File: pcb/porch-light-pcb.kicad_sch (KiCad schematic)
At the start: 1 part

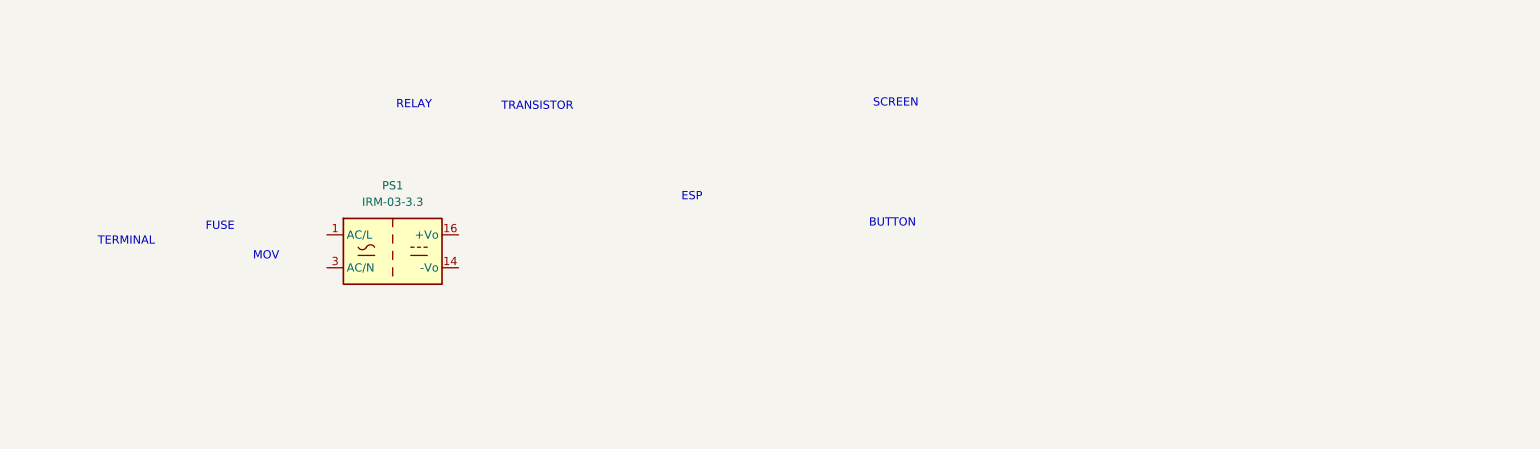
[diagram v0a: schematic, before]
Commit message: esp32 symbol and footprint
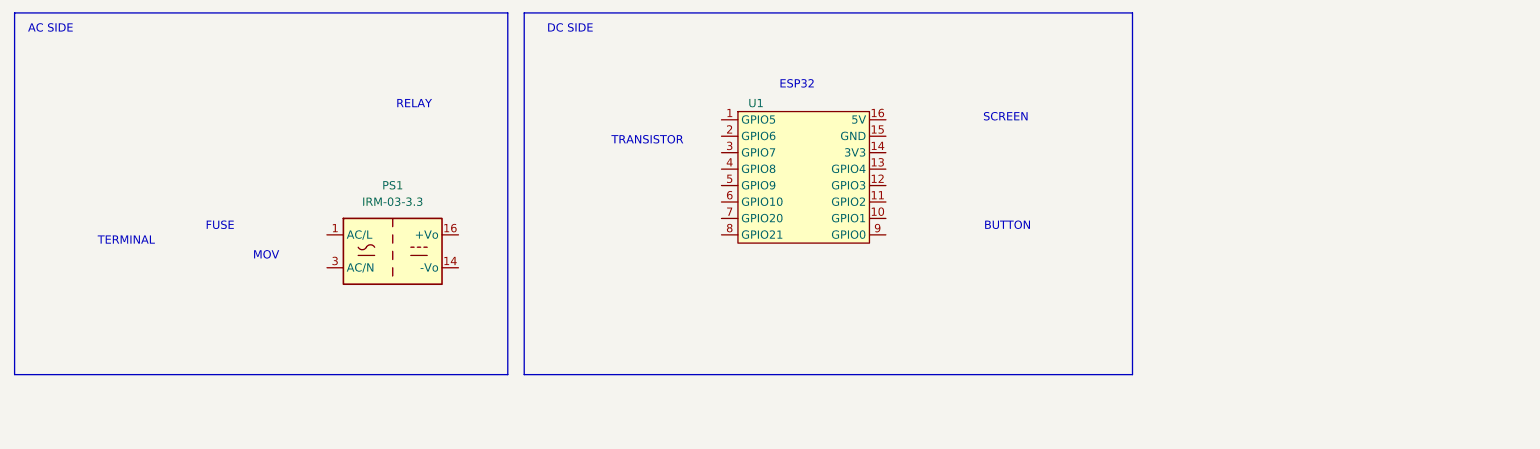
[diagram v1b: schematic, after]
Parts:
- added U1: ~, TENSTAR:TENSTAR_ESP32-C3-SUPERMINI, symbol TENSTAR:TENSTAR_ESP32-C3-SUPERMINI
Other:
- note added: "AC SIDE"
- note added: "DC SIDE"
- note added: "ESP32"
- note removed: "ESP"
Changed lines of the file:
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@@
 	(generator_version "9.0")
 	(paper "A4")
+	(rectangle
+		(start 92.71 12.7)
+		(end 186.69 68.58)
+		(stroke
+			(width 0)
+			(type default)
+		)
+		(fill
+			(type none)
+		)
+	)
+	(rectangle
+		(start 13.97 12.7)
+		(end 90.17 68.58)
+		(stroke
+			(width 0)
+			(type default)
+		)
+		(fill
+			(type none)
+		)
+	)
 	(text "FUSE"
 		(exclude_from_sim no)
@@
 		)
 	)
+	(text "DC SIDE\n"
+		(exclude_from_sim no)
+		(at 99.822 15.24 0)
+		(effects
+			(font
+				(size 1.27 1.27)
+			)
+		)
+	)
 	(text "MOV"
 		(exclude_from_sim no)
@@
 	(text "TRANSISTOR"
 		(exclude_from_sim no)
-		(at 94.742 27.178 0)
+		(at 111.76 32.512 0)
+		(effects
+			(font
+				(size 1.27 1.27)
+			)
+		)
+	)
+	(text "AC SIDE\n"
+		(exclude_from_sim no)
+		(at 19.558 15.24 0)
 		(effects
 			(font
@@
 	(text "SCREEN"
 		(exclude_from_sim no)
-		(at 150.114 26.67 0)
-		(effects
-			(font
-				(size 1.27 1.27)
-			)
-		)
-	)
-	(text "ESP\n"
-		(exclude_from_sim no)
-		(at 118.618 41.148 0)
+		(at 167.132 28.956 0)
+		(effects
+			(font
+				(size 1.27 1.27)
+			)
+		)
+	)
+	(text "ESP32"
+		(exclude_from_sim no)
+		(at 134.874 23.876 0)
 		(effects
 			(font
@@
 	(text "BUTTON\n"
 		(exclude_from_sim no)
-		(at 149.606 45.212 0)
-		(effects
-			(font
-				(size 1.27 1.27)
-			)
-		)
+		(at 167.386 45.72 0)
+		(effects
+			(font
+				(size 1.27 1.27)
+			)
+		)
+	)
+	(symbol
+		(lib_id "TENSTAR:TENSTAR_ESP32-C3-SUPERMINI")
+		(at 135.89 39.37 0)
+		(unit 1)
+		(exclude_from_sim no)
+		(in_bom yes)
+		(on_board yes)
+		(dnp no)
+		(property "Reference" "U1"
+			(at 128.524 26.67 0)
+			(effects
+				(font
+					(size 1.27 1.27)
+				)
+			)
+		)
+		(property "Value" "~"
+			(at 135.89 26.416 0)
+			(effects
+				(font
+					(size 1.27 1.27)
+				)
+				(hide yes)
+			)
+		)
+		(property "Footprint" "TENSTAR:TENSTAR_ESP32-C3-SUPERMINI"
+			(at 135.89 53.086 0)
+			(effects
+				(font
+					(size 1.27 1.27)
+				)
+				(hide yes)
+			)
+		)
+		(property "Datasheet" "https://www.waveshare.com/wiki/ESP32-C3-Zero"
+			(at 135.636 55.626 0)
+			(effects
+				(font
+					(size 1.27 1.27)
+				)
+				(hide yes)
+			)
+		)
+		(property "Description" ""
+			(at 125.73 29.21 0)
+			(effects
+				(font
+					(size 1.27 1.27)
+				)
+				(hide yes)
+			)
+		)
+		(pin "8"
+		)
+		(pin "6"
+		)
+		(pin "14"
+		)
+		(pin "7"
+		)
+		(pin "2"
+		)
+		(pin "1"
+		)
+		(pin "13"
+		)
+		(pin "4"
+		)
+		(pin "11"
+		)
+		(pin "3"
+		)
+		(pin "10"
+		)
+		(pin "12"
+		)
+		(pin "5"
+		)
+		(pin "15"
+		)
+		(pin "9"
+		)
+		(pin "16"
+		)
+		(instances
+			(project "porch-light-pcb"
+				(path "/c90725bf-bd5a-4426-8225-f7c4cfb17e78"
+					(reference "U1")
+					(unit 1)
+				)
+			)
+		)

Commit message: preliminary circuit design
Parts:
- added C1: 220uF, Capacitor_THT:CP_Radial_D5.0mm_P2.50mm, symbol Device:C_Polarized
- added C2: 0.1uF, Capacitor_SMD:C_0603_1608Metric_Pad1.08x0.95mm_HandSolder, symbol Device:C
- added F1: 0HAAL1000-02, symbol Device:Fuse
- added J1: Screw_Terminal_01x02, symbol Connector:Screw_Terminal_01x02
- added J2: Conn_01x02, Connector_PinHeader_2.54mm:PinHeader_1x02_P2.54mm_Vertical, symbol Connector_Generic:Conn_01x02
- added J4: Screw_Terminal_01x01, symbol Connector:Screw_Terminal_01x01
- added K1: PRY2-3V-450-1A-EF, PRY2_3V_450_1A_EF:RELAY_PRY2-3V-450-1A-EF, symbol PRY2-3V-450-1A-EF:PRY2-3V-450-1A-EF
- added Q1: PN2222A, Package_TO_SOT_THT:TO-92_Inline, symbol Transistor_BJT:PN2222A
- added R1: 270R, symbol Device:R_US
- added RV1: V150LA10AP, symbol Device:Varistor
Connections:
- net GND: now reaches U1.15 (GND)
- net GND: now also PS1.14 (-Vo), C1.2, C2.2, J2.2 (Pin_2), Q1.1 (E)
- net +3.3V: now reaches U1.16 (5V)
- net +3.3V: now also PS1.16 (+Vo), C1.1, C2.1, K1.COIL1
- net BUTTON_GPIO: now reaches U1.9 (GPIO0)
- net BUTTON_GPIO: now also J2.1 (Pin_1)
- net at PS1.1 (AC/L): now also F1.2, RV1.1
- net at PS1.3 (AC/N): now also J1.2 (Pin_2), RV1.2
- new net: F1.1, J1.1 (Pin_1), K1.NO
- new net: Q1.2 (B), R1.2
- new net: J4.1 (Pin_1), K1.COM
- new net RELAY_GND: K1.COIL2, Q1.3 (C)
- new net RELAY_GPIO: R1.1
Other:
- note added: "250VAC 2A Slow blow"
- note added: "AC IN"
- note added: "Placed very close to ESP32"
- note added: "TO LIGHT"
- note removed: "FUSE"
- note removed: "MOV"
- note removed: "SCREEN"
- note removed: "TERMINAL"
- moved on the sheet: PS1, U1

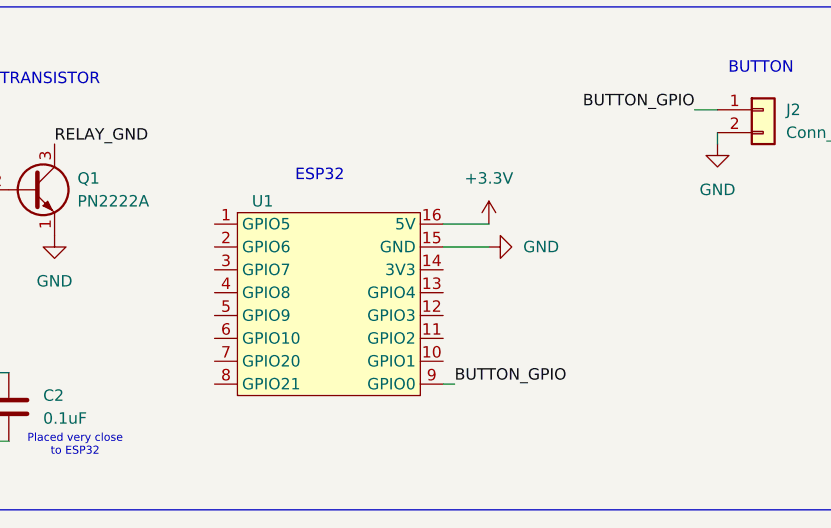
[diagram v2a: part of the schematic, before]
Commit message: relay_gpio connection
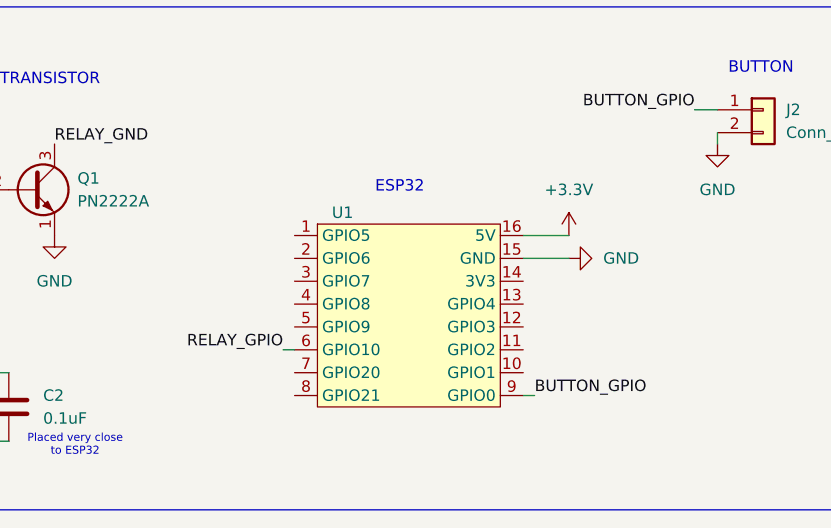
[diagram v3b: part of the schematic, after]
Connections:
- net RELAY_GPIO: now also U1.6 (GPIO10)
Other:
- moved on the sheet: U1
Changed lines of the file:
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@@
 	(text "ESP32"
 		(exclude_from_sim no)
-		(at 160.274 31.496 0)
+		(at 169.164 32.766 0)
 		(effects
 			(font
@@
 	(wire
 		(pts
-			(xy 173.99 36.83) (xy 179.07 36.83)
+			(xy 182.88 38.1) (xy 187.96 38.1)
 		)
 		(stroke
@@
 	(wire
 		(pts
+			(xy 156.21 50.8) (xy 157.48 50.8)
+		)
+		(stroke
+			(width 0)
+			(type default)
+		)
+	)
+	(wire
+		(pts
 			(xy 41.91 53.34) (xy 46.99 53.34)
 		)
@@
 	(wire
 		(pts
-			(xy 173.99 39.37) (xy 179.07 39.37)
+			(xy 182.88 40.64) (xy 187.96 40.64)
 		)
 		(stroke
@@
 	(wire
 		(pts
-			(xy 175.26 54.61) (xy 173.99 54.61)
+			(xy 184.15 55.88) (xy 182.88 55.88)
 		)
 		(stroke
@@
 		)
 	)
+	(label "RELAY_GPIO"
+		(at 156.21 50.8 180)
+		(effects
+			(font
+				(size 1.27 1.27)
+			)
+			(justify right bottom)
+		)
+	)
 	(label "RELAY_GND"
 		(at 130.81 27.94 0)
@@
 	)
 	(label "BUTTON_GPIO"
-		(at 175.26 54.61 0)
+		(at 184.15 55.88 0)
 		(effects
 			(font
@@
 	(symbol
 		(lib_id "power:GND")
-		(at 179.07 39.37 90)
+		(at 187.96 40.64 90)
 		(unit 1)
 		(exclude_from_sim no)
@@
 		(fields_autoplaced yes)
 		(property "Reference" "#PWR06"
-			(at 185.42 39.37 0)
+			(at 194.31 40.64 0)
 			(effects
 				(font
@@
 		)
 		(property "Value" "GND"
-			(at 182.88 39.3699 90)
+			(at 191.77 40.6399 90)
 			(effects
 				(font
@@
 		)
 		(property "Footprint" ""
-			(at 179.07 39.37 0)
+			(at 187.96 40.64 0)
 			(effects
 				(font
@@
 		)
 		(property "Datasheet" ""
-			(at 179.07 39.37 0)
+			(at 187.96 40.64 0)
 			(effects
 				(font
@@
 		)
 		(property "Description" "Power symbol creates a global label with name \"GND\" , ground"
-			(at 179.07 39.37 0)
+			(at 187.96 40.64 0)
 			(effects
 				(font
@@
 	(symbol
 		(lib_id "TENSTAR:TENSTAR_ESP32-C3-SUPERMINI")
-		(at 161.29 46.99 0)
+		(at 170.18 48.26 0)
 		(unit 1)
 		(exclude_from_sim no)
@@
 		(dnp no)
 		(property "Reference" "U1"
-			(at 153.924 34.29 0)
+			(at 162.814 35.56 0)
 			(effects
 				(font
@@
 		)
 		(property "Value" "~"
-			(at 161.29 34.036 0)
+			(at 170.18 35.306 0)
 			(effects
 				(font
@@
 		)
 		(property "Footprint" "TENSTAR:TENSTAR_ESP32-C3-SUPERMINI"
-			(at 161.29 60.706 0)
+			(at 170.18 61.976 0)
 			(effects
 				(font
@@
 		)
 		(property "Datasheet" "https://www.waveshare.com/wiki/ESP32-C3-Zero"
-			(at 161.036 63.246 0)
+			(at 169.926 64.516 0)
 			(effects
 				(font
@@
 		)
 		(property "Description" ""
-			(at 151.13 36.83 0)
+			(at 160.02 38.1 0)
 			(effects
 				(font
@@
 	(symbol
 		(lib_id "power:+3.3V")
-		(at 179.07 36.83 0)
+		(at 187.96 38.1 0)
 		(unit 1)
 		(exclude_from_sim no)
@@
 		(fields_autoplaced yes)
 		(property "Reference" "#PWR05"
-			(at 179.07 40.64 0)
+			(at 187.96 41.91 0)
 			(effects
 				(font
@@
 		)
 		(property "Value" "+3.3V"
-			(at 179.07 31.75 0)
+			(at 187.96 33.02 0)
 			(effects
 				(font
@@
 		)
 		(property "Footprint" ""
-			(at 179.07 36.83 0)
+			(at 187.96 38.1 0)
 			(effects
 				(font
@@
 		)
 		(property "Datasheet" ""
-			(at 179.07 36.83 0)
+			(at 187.96 38.1 0)
 			(effects
 				(font
@@
 		)
 		(property "Description" "Power symbol creates a global label with name \"+3.3V\""
-			(at 179.07 36.83 0)
-			(effects
-				(font
+			(at 187.96 38.1 0)
+			(effects
+				(font

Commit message: terminal block chosen
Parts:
- removed J1: Screw_Terminal_01x02, symbol Connector:Screw_Terminal_01x02
- removed J4: Screw_Terminal_01x01, symbol Connector:Screw_Terminal_01x01
- added J1: HA0300500000G, CONN_HA0300500000G_AMP, symbol 2026-08-06_05-33-22:HA0300500000G
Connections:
- net AC_LIVE: now reaches F1.1, K1.NO
- net AC_LIVE: now also J1.3, J1.4
- net at K1.COM: now also J1.5, J1.6
- net AC_NEUTRAL: now reaches PS1.3 (AC/N), RV1.2
- net AC_NEUTRAL: now also J1.1, J1.2
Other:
- moved on the sheet: C1, C2, F1, J2, K1, PS1, Q1, R1, RV1, U1

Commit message: footprint assignment
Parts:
- F1: footprint (none) -> 0HAAL1000_02:FUSRR508W60L840T400H810B
- J1: footprint CONN_HA0300500000G_AMP -> HA0300500000G:CONN_HA0300500000G_AMP
- R1: footprint (none) -> Resistor_THT:R_Axial_DIN0207_L6.3mm_D2.5mm_P10.16mm_Horizontal
- RV1: footprint (none) -> Varistor:RV_Disc_D15.5mm_W5.4mm_P7.5mm
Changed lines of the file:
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@@
 			)
 		)
-		(property "Footprint" "CONN_HA0300500000G_AMP"
+		(property "Footprint" "HA0300500000G:CONN_HA0300500000G_AMP"
 			(at 30.48 62.23 0)
 			(effects
@@
 			)
 		)
-		(property "Footprint" ""
+		(property "Footprint" "0HAAL1000_02:FUSRR508W60L840T400H810B"
 			(at 57.15 56.388 90)
 			(effects
@@
 			)
 		)
-		(property "Footprint" ""
+		(property "Footprint" "Resistor_THT:R_Axial_DIN0207_L6.3mm_D2.5mm_P10.16mm_Horizontal"
 			(at 138.684 33.274 90)
 			(effects
@@
 			)
 		)
-		(property "Footprint" ""
+		(property "Footprint" "Varistor:RV_Disc_D15.5mm_W5.4mm_P7.5mm"
 			(at 64.262 58.42 90)
 			(effects

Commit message: intial board layout, chose some smaller parts
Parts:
- removed J1: HA0300500000G, HA0300500000G:CONN_HA0300500000G_AMP, symbol 2026-08-06_05-33-22:HA0300500000G
- added J1: 1-2834011-3, CONN_1-2834011-3_TEC, symbol 2026-08-07_02-42-31:1-2834011-3
- RV1: value V150LA10AP -> V150LA5P; footprint Varistor:RV_Disc_D15.5mm_W5.4mm_P7.5mm -> Varistor:RV_Disc_D12mm_W5.8mm_P7.5mm
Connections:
- net AC_LIVE: now also J1.2
- net AC_NEUTRAL: now also J1.1
- net at K1.COM: now also J1.3
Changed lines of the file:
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@@
 	(text "AC IN\n"
 		(exclude_from_sim no)
-		(at 21.844 39.116 0)
+		(at 21.336 44.196 0)
 		(effects
 			(font
@@
 	)
 	(junction
-		(at 30.48 54.61)
-		(diameter 0)
-		(color 0 0 0 0)
-	)
-	(junction
 		(at 137.16 54.61)
-		(diameter 0)
-		(color 0 0 0 0)
-	)
-	(junction
-		(at 30.48 49.53)
 		(diameter 0)
 		(color 0 0 0 0)
@@
 	)
 	(junction
-		(at 30.48 62.23)
-		(diameter 0)
-		(color 0 0 0 0)
-	)
-	(junction
 		(at 48.26 43.18)
 		(diameter 0)
@@
 	(wire
 		(pts
+			(xy 29.21 57.15) (xy 48.26 57.15)
+		)
+		(stroke
+			(width 0)
+			(type default)
+		)
+	)
+	(wire
+		(pts
 			(xy 220.98 25.4) (xy 223.52 25.4)
 		)
@@
 	(wire
 		(pts
-			(xy 44.45 26.67) (xy 81.28 26.67)
+			(xy 44.45 59.69) (xy 44.45 62.23)
+		)
+		(stroke
+			(width 0)
+			(type default)
+		)
+	)
+	(wire
+		(pts
+			(xy 43.18 26.67) (xy 81.28 26.67)
 		)
 		(stroke
@@
 	(wire
 		(pts
-			(xy 44.45 49.53) (xy 44.45 26.67)
+			(xy 43.18 54.61) (xy 43.18 26.67)
 		)
 		(stroke
@@
 	(wire
 		(pts
-			(xy 30.48 49.53) (xy 44.45 49.53)
+			(xy 29.21 54.61) (xy 43.18 54.61)
 		)
 		(stroke
@@
 	(wire
 		(pts
-			(xy 30.48 62.23) (xy 44.45 62.23)
-		)
-		(stroke
-			(width 0)
-			(type default)
-		)
-	)
-	(wire
-		(pts
 			(xy 223.52 29.21) (xy 223.52 27.94)
 		)
@@
 	(wire
 		(pts
-			(xy 30.48 49.53) (xy 30.48 52.07)
-		)
-		(stroke
-			(width 0)
-			(type default)
-		)
-	)
-	(wire
-		(pts
-			(xy 30.48 59.69) (xy 30.48 62.23)
+			(xy 29.21 59.69) (xy 44.45 59.69)
 		)
 		(stroke
@@
 	(wire
 		(pts
-			(xy 30.48 54.61) (xy 30.48 57.15)
-		)
-		(stroke
-			(width 0)
-			(type default)
-		)
-	)
-	(wire
-		(pts
 			(xy 201.93 41.91) (xy 207.01 41.91)
 		)
@@
 	(wire
 		(pts
+			(xy 48.26 57.15) (xy 48.26 54.61)
+		)
+		(stroke
+			(width 0)
+			(type default)
+		)
+	)
+	(wire
+		(pts
 			(xy 129.54 62.23) (xy 137.16 62.23)
 		)
@@
 		(pts
 			(xy 106.68 59.69) (xy 106.68 60.96)
-		)
-		(stroke
-			(width 0)
-			(type default)
-		)
-	)
-	(wire
-		(pts
-			(xy 30.48 54.61) (xy 48.26 54.61)
 		)
 		(stroke
@@
 	)
 	(symbol
-		(lib_id "2026-08-06_05-33-22:HA0300500000G")
-		(at 30.48 62.23 180)
-		(unit 1)
-		(exclude_from_sim no)
-		(in_bom yes)
-		(on_board yes)
-		(dnp no)
-		(property "Reference" "J1"
-			(at 21.336 44.958 0)
-			(effects
-				(font
-					(size 1.524 1.524)
-				)
-			)
-		)
-		(property "Value" "HA0300500000G"
-			(at 24.638 68.58 0)
-			(effects
-				(font
-					(size 1.524 1.524)
-				)
-			)
-		)
-		(property "Footprint" "HA0300500000G:CONN_HA0300500000G_AMP"
-			(at 30.48 62.23 0)
-			(effects
-				(font
-					(size 1.27 1.27)
-					(italic yes)
-				)
-				(hide yes)
-			)
-		)
-		(property "Datasheet" "HA0300500000G"
-			(at 30.48 62.23 0)
-			(effects
-				(font
-					(size 1.27 1.27)
-					(italic yes)
-				)
-				(hide yes)
-			)
-		)
-		(property "Description" ""
-			(at 30.48 62.23 0)
-			(effects
-				(font
-					(size 1.27 1.27)
-				)
-				(hide yes)
-			)
-		)
-		(pin "2"
-		)
-		(pin "1"
-		)
-		(pin "6"
-		)
-		(pin "3"
-		)
-		(pin "5"
-		)
-		(pin "4"
-		)
-		(instances
-			(project "porch-light-pcb"
-				(path "/c90725bf-bd5a-4426-8225-f7c4cfb17e78"
-					(reference "J1")
-					(unit 1)
-				)
-			)
-		)
-	)
-	(symbol
 		(lib_id "power:GND")
 		(at 137.16 62.23 0)
@@
 	)
 	(symbol
+		(lib_id "2026-08-07_02-42-31:1-2834011-3")
+		(at 29.21 59.69 180)
+		(unit 1)
+		(exclude_from_sim no)
+		(in_bom yes)
+		(on_board yes)
+		(dnp no)
+		(property "Reference" "J1"
+			(at 20.32 46.99 0)
+			(effects
+				(font
+					(size 1.524 1.524)
+				)
+			)
+		)
+		(property "Value" "1-2834011-3"
+			(at 22.86 49.784 0)
+			(effects
+				(font
+					(size 1.524 1.524)
+				)
+			)
+		)
+		(property "Footprint" "CONN_1-2834011-3_TEC"
+			(at 29.21 59.69 0)
+			(effects
+				(font
+					(size 1.27 1.27)
+					(italic yes)
+				)
+				(hide yes)
+			)
+		)
+		(property "Datasheet" "https://www.te.com/commerce/DocumentDelivery/DDEController?Action=srchrtrv&DocNm=1-1773872-7_ModularScrewlessTB_CN&DocType=Data+Sheet&DocLang=Chinese+%28Simplified%29&PartCntxt=1-2834011-3&DocFormat=pdf"
+			(at 29.21 59.69 0)
+			(effects
+				(font
+					(size 1.27 1.27)
+					(italic yes)
+				)
+				(hide yes)
+			)
+		)
+		(property "Description" ""
+			(at 29.21 59.69 0)
+			(effects
+				(font
+					(size 1.27 1.27)
+				)
+				(hide yes)
+			)
+		)
+		(pin "3"
+		)
+		(pin "2"
+		)
+		(pin "1"
+		)
+		(instances
+			(project "porch-light-pcb"
+				(path "/c90725bf-bd5a-4426-8225-f7c4cfb17e78"
+					(reference "J1")
+					(unit 1)
+				)
+			)
+		)
+	)
+	(symbol
 		(lib_id "power:GND")
 		(at 207.01 41.91 90)
@@
 			)
 		)
-		(property "Value" "V150LA10AP"
+		(property "Value" "V150LA5P"
 			(at 68.58 59.8832 0)
 			(effects
@@
 			)
 		)
-		(property "Footprint" "Varistor:RV_Disc_D15.5mm_W5.4mm_P7.5mm"
+		(property "Footprint" "Varistor:RV_Disc_D12mm_W5.8mm_P7.5mm"
 			(at 64.262 58.42 90)
 			(effects

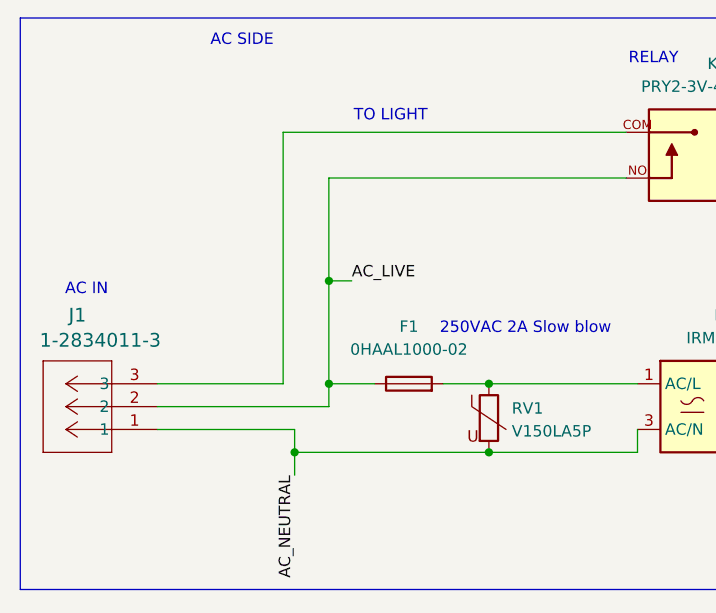
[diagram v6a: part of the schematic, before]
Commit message: fixed netclasses
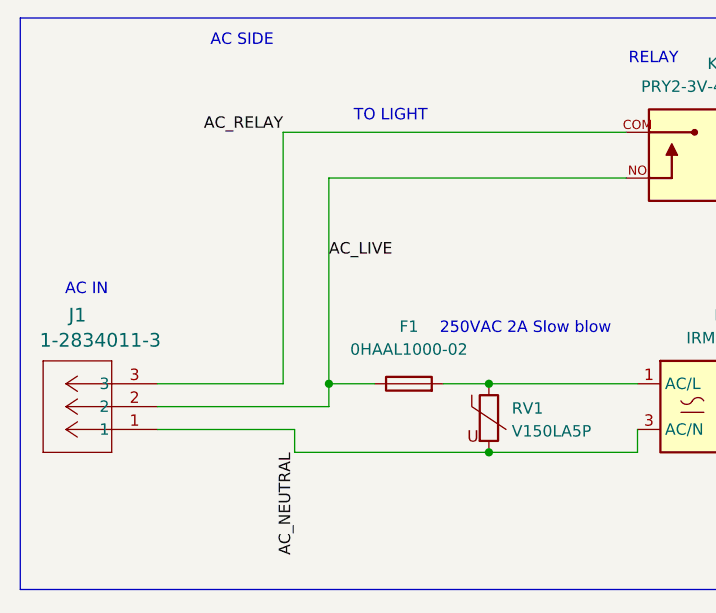
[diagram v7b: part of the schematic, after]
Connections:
- net AC_RELAY: now reaches J1.3, K1.COM
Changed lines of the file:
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@@
-	)
-	(junction
-		(at 44.45 62.23)
-		(diameter 0)
-		(color 0 0 0 0)
 	)
 	(junction
@@
 	)
 	(junction
-		(at 48.26 43.18)
-		(diameter 0)
-		(color 0 0 0 0)
-	)
-	(junction
 		(at 48.26 54.61)
 		(diameter 0)
@@
 	(wire
 		(pts
-			(xy 44.45 64.77) (xy 44.45 62.23)
-		)
-		(stroke
-			(width 0)
-			(type default)
-		)
-	)
-	(wire
-		(pts
-			(xy 48.26 31.75) (xy 48.26 43.18)
-		)
-		(stroke
-			(width 0)
-			(type default)
-		)
-	)
-	(wire
-		(pts
 			(xy 101.6 26.67) (xy 106.68 26.67)
 		)
@@
 	(wire
 		(pts
-			(xy 48.26 43.18) (xy 48.26 54.61)
+			(xy 48.26 31.75) (xy 48.26 54.61)
 		)
 		(stroke
@@
 	(wire
 		(pts
-			(xy 50.8 43.18) (xy 48.26 43.18)
-		)
-		(stroke
-			(width 0)
-			(type default)
-		)
-	)
-	(wire
-		(pts
 			(xy 43.18 54.61) (xy 43.18 26.67)
 		)
@@
 			(width 0)
 			(type default)
-		)
-	)
-	(label "AC_NEUTRAL"
-		(at 44.45 64.77 270)
-		(effects
-			(font
-				(size 1.27 1.27)
-			)
-			(justify right bottom)
 		)
 	)
@@
 		)
 	)
+	(label "AC_RELAY"
+		(at 43.18 26.67 180)
+		(effects
+			(font
+				(size 1.27 1.27)
+			)
+			(justify right bottom)
+		)
+	)
+	(label "AC_NEUTRAL"
+		(at 44.45 62.23 270)
+		(effects
+			(font
+				(size 1.27 1.27)
+			)
+			(justify right bottom)
+		)
+	)
 	(label "AC_LIVE"
-		(at 50.8 43.18 0)
-		(effects
-			(font
+		(at 48.26 40.64 0)
+		(effects
+			(font

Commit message: finished routing
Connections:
- net AC_FILTERED: now reaches F1.2, PS1.1 (AC/L), RV1.1
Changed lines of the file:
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@@
 	(text "250VAC 2A Slow blow\n"
 		(exclude_from_sim no)
-		(at 70.104 48.514 0)
+		(at 61.214 46.99 0)
 		(effects
 			(font
@@
 		)
 	)
+	(label "AC_FILTERED"
+		(at 78.74 54.61 90)
+		(effects
+			(font
+				(size 1.27 1.27)
+			)
+			(justify left bottom)
+		)
+	)
